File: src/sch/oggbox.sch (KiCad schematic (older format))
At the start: 143 parts, among them IC1 VS1053, IC2 MCP73831T, IC3 SD_CARD, IC4 MCP1603T, IC5 STM32F103RBT, IC7 TPS76318, IC8 TPS76328, IC9 MCP102, P10 HPHN, P2 USB, P5 CONN_4, P6 CONN_28, P7 FTDI, P8 JTAG, P9 LINE, Q1 BC817, Q2 BC817, Q3 BSH121, Q4 BSH121, SW1 VOL_UP, SW10 UP, SW11 HOLD, SW2 VOL_DN, SW3 RESET, SW4 MENU, SW5 SET, SW7 DOWN, SW8 LEFT, SW9 RIGHT, X1 12.288MHz, X2 32768Hz, X3 8MHz

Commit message: More routing.  Some schematic fixes, now 3.0V not 3.3V
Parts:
- removed IC4: MCP1603T, symbol MCP1603T
- removed L2: 4.7u, symbol INDUCTOR
- removed SW10: UP, symbol SW_PUSH
- removed SW4: MENU, symbol SW_PUSH
- removed SW5: SET, symbol SW_PUSH
- removed SW7: DOWN, symbol SW_PUSH
- removed SW8: LEFT, symbol SW_PUSH
- removed SW9: RIGHT, symbol SW_PUSH
- added IC4: MCP1802T-3002I-OT, symbol MCP1802T-3002I-OT
- added SW10: UP, symbol SW_PUSH4
- added SW4: MENU, symbol SW_PUSH4
- added SW5: SET, symbol SW_PUSH4
- added SW7: DOWN, symbol SW_PUSH4
- added SW8: LEFT, symbol SW_PUSH4
- added SW9: RIGHT, symbol SW_PUSH4
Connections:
- net labels added: +3.0V, HOLD
- net labels removed: +3.3V, Lx1
- wire segments 502 -> 513
- no-connect marks 10 -> 14
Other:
- moved on the sheet: C30, P8, R48, R49, R50, R51, R52, R57

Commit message: 100% routed!
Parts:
- removed P10: HPHN, symbol CONN_4
- removed P9: LINE, symbol CONN_4
- removed SW11: HOLD, symbol SWITCH_INV
- added P10, P9: JACK_LUMBERG_1503_13_VP3, symbol JACK_LUMBERG_1503_13_VP3
- added SW11: HOLD, symbol SWITCH_INV_MECH
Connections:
- wire segments 513 -> 519
- no-connect marks 14 -> 19

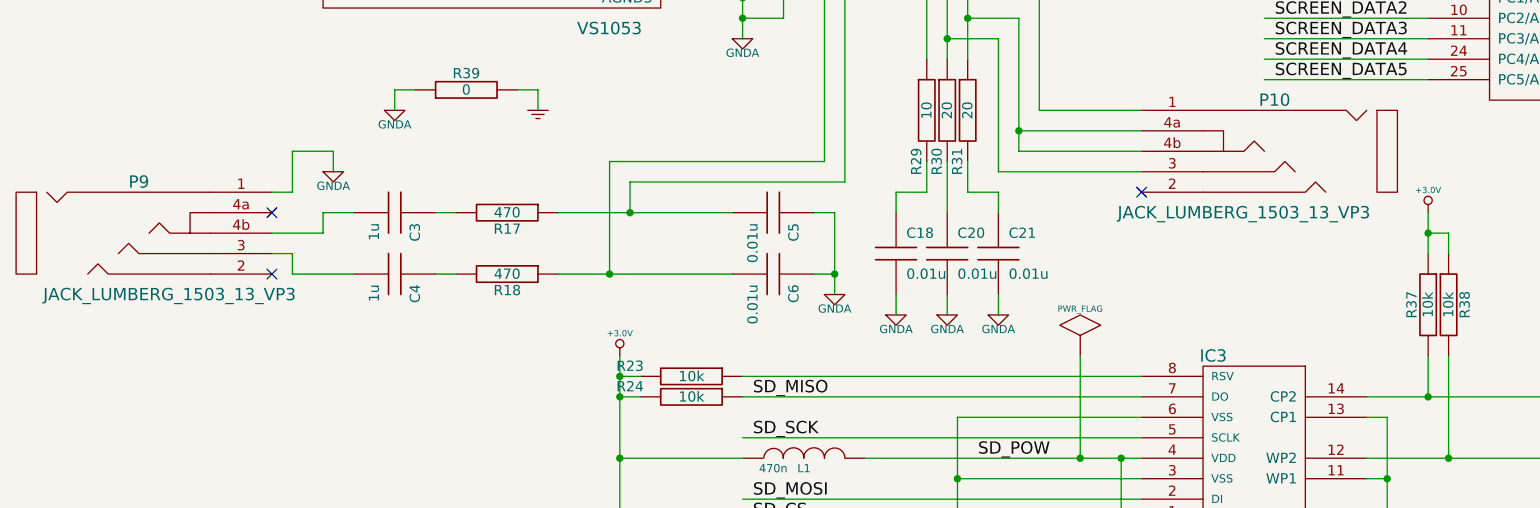
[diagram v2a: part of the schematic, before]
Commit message: Tidied up all the silk screen should be ready for manufacture.
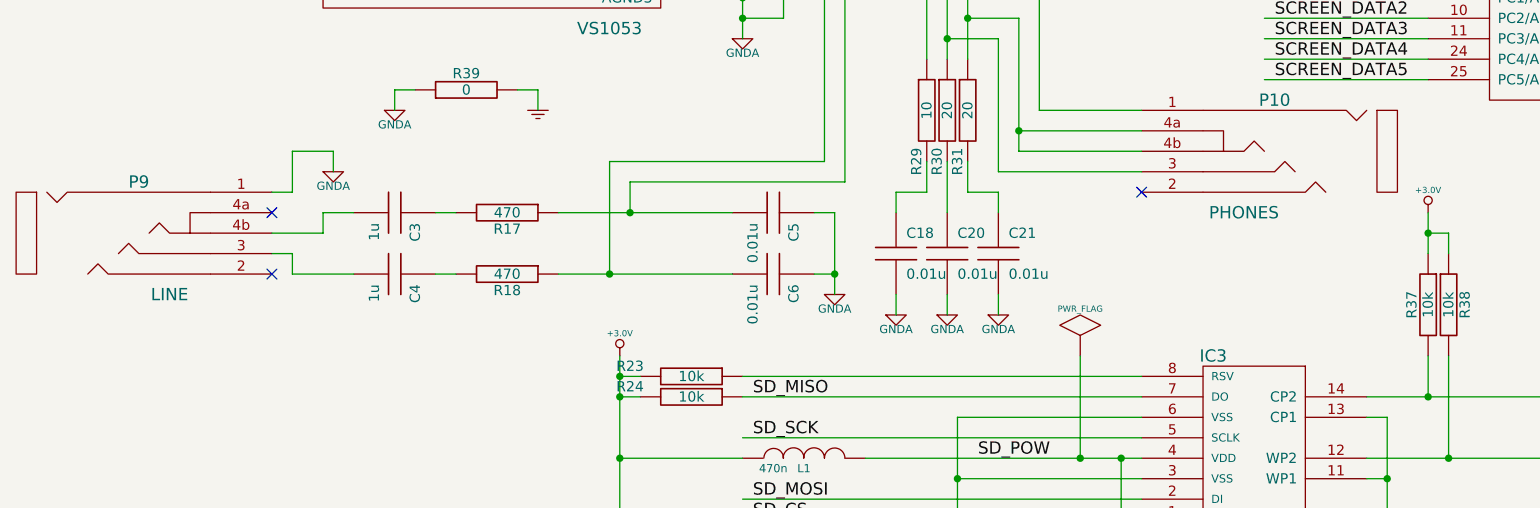
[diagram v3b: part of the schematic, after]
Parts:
- P10: value JACK_LUMBERG_1503_13_VP3 -> PHONES
- P9: value JACK_LUMBERG_1503_13_VP3 -> LINE
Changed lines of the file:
@@
-EESchema Schematic File Version 2  date Tue 22 May 2012 16:03:11 BST
+EESchema Schematic File Version 2  date Wed 23 May 2012 14:46:38 BST
 LIBS:74xx
 LIBS:adc-dac
@@
 Sheet 1 1
 Title ""
-Date "22 may 2012"
+Date "23 may 2012"
 Rev ""
 Comp ""
@@
 P 6550 6050
 F 0 "P10" H 6400 6350 60  0000 C CNN
-F 1 "JACK_LUMBERG_1503_13_VP3" H 6550 5800 60  0000 C CNN
+F 1 "PHONES" H 6550 5800 60  0000 C CNN
 	1    6550 6050
 	-1   0    0    -1
@@
 P 1300 6450
 F 0 "P9" H 1150 6750 60  0000 C CNN
-F 1 "JACK_LUMBERG_1503_13_VP3" H 1300 6200 60  0000 C CNN
+F 1 "LINE" H 1300 6200 60  0000 C CNN
 	1    1300 6450
 	1    0    0    -1

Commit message: Back annotated footprints for faster BOM generation
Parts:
- B1: footprint (none) -> JUMPER
- C1, C10, C11, C12, C13, C14, C15, C16, C17, C18, C19, C2, C20, C21, C22, C24, C25, C26, C27, C28, C29, C3, C30, C32, C33, C34, C35, C36, C37, C39, C4, C40, C41, C42, C43, C44, C45, C46, C47, C48, C49, C5, C50, C51, C52, C53, C54, C55, C6, C7, C8, C9, R1, R10, R11, R12, R13, R14, R15, R16, R17, R18, R19, R2, R20, R21, R22, R23, R24, R25, R26, R27, R28, R29, R3, R30, R31, R32, R33, R34, R35, R36, R37, R38, R39, R4, R40, R41, R42, R43, R44, R46, R48, R49, R5, R50, R51, R52, R53, R54, R56, R57, R6, R7, R8, R9: footprint (none) -> SM0805
- C23, L1: footprint (none) -> SM1206
- D1, IC9, Q1, Q2, Q3, Q4: footprint (none) -> SOT23
- IC1: footprint (none) -> LQFP48
- IC2, IC4, IC7, IC8: footprint (none) -> SOT23-5
- IC3: footprint (none) -> SD_CARD9186158
- IC5: footprint (none) -> LQFP64
- P10, P9: footprint (none) -> JACK_LUMBERG_1503_13_VP3
- P2: footprint (none) -> MICRO_USB_1568026
- P5: footprint (none) -> BTHQ128064AVD1
- P6: footprint (none) -> AMP_FPC_28_05MM
- P7: footprint (none) -> HEADER_6
- P8: footprint (none) -> header_smd
- SW1, SW2, SW3: footprint (none) -> SW_B3U-3000P-B
- SW10, SW4, SW5, SW7, SW8, SW9: footprint (none) -> SW_EVQQ2P03W
- SW11: footprint (none) -> PCM12SMTR
- X1, X3: footprint (none) -> HC49SM
- X2: footprint (none) -> CFS206

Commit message: Committed RevA to PDF and started moding schematic for RevB
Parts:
- added Q?: BSH121, symbol BSH121
- added R? (x2): 10k, symbol R
- added R?: 22, symbol R
- C18: value 0.01u -> 0.047u
- C7: value 0.1u -> 1u
- R29: value 10 -> 22
- R30, R31: value 20 -> 22
- R53, R54: value 27 -> 22
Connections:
- net labels added: READ_BATT
- net labels removed: AUX_PWR
- wire segments 519 -> 530
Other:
- moved on the sheet: B1, C19, C22, C26, C30, C55, IC2, IC4, IC9, Q4, R27, R28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

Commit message: Working on RevB schematic a bit more.  PSU redesign.
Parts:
- removed C26, C30: 4.7u, SM0805, symbol CAPAPOL
- added C26, C30: 4.7u, symbol C
- R27, R28: value 100k -> 1k
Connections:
- wire segments 530 -> 526
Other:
- moved on the sheet: B1, C19, C22, C43, C44, C45, C55, IC2, IC4, IC9, P7, Q4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

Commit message: Preparing to lay out Rev B board
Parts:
- gave numbers to parts that had none: 4

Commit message: Re-routed the power supply control for RevB
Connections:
- net labels added: RBG
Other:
- moved on the sheet: Q5
